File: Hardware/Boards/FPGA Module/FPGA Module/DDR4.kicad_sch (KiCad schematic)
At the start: 0 parts

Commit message: FPGA Module Schematic work
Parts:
- added U17: MT40A512M16LY-075:E, FPGA Module:BGA96C80P9X16_750X1350X120, symbol FPGA Module:MT40A512M16LY-075{colon}E

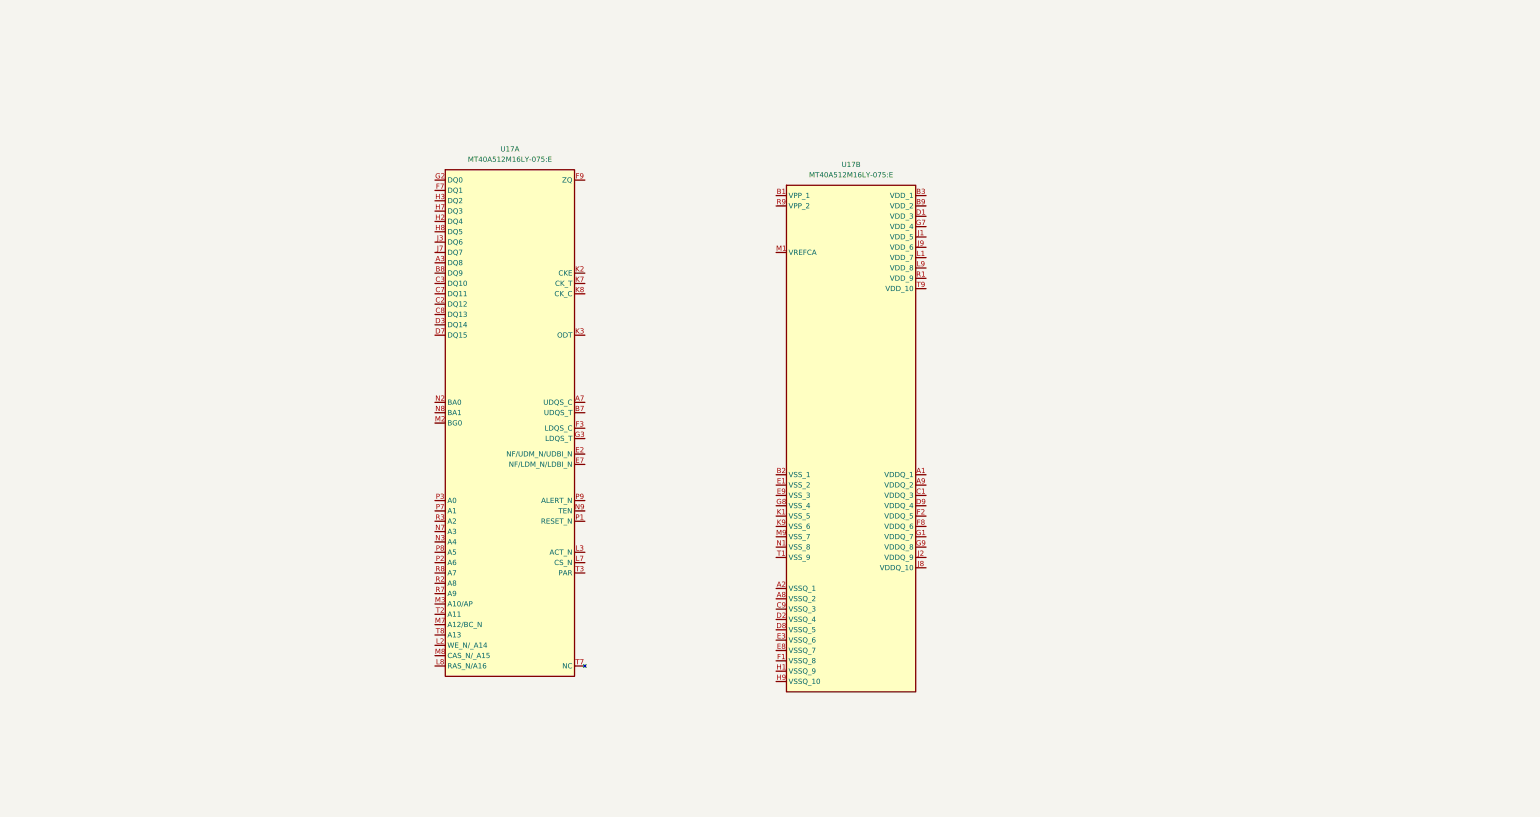
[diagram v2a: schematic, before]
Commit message: Added DDR sch in FPGA module
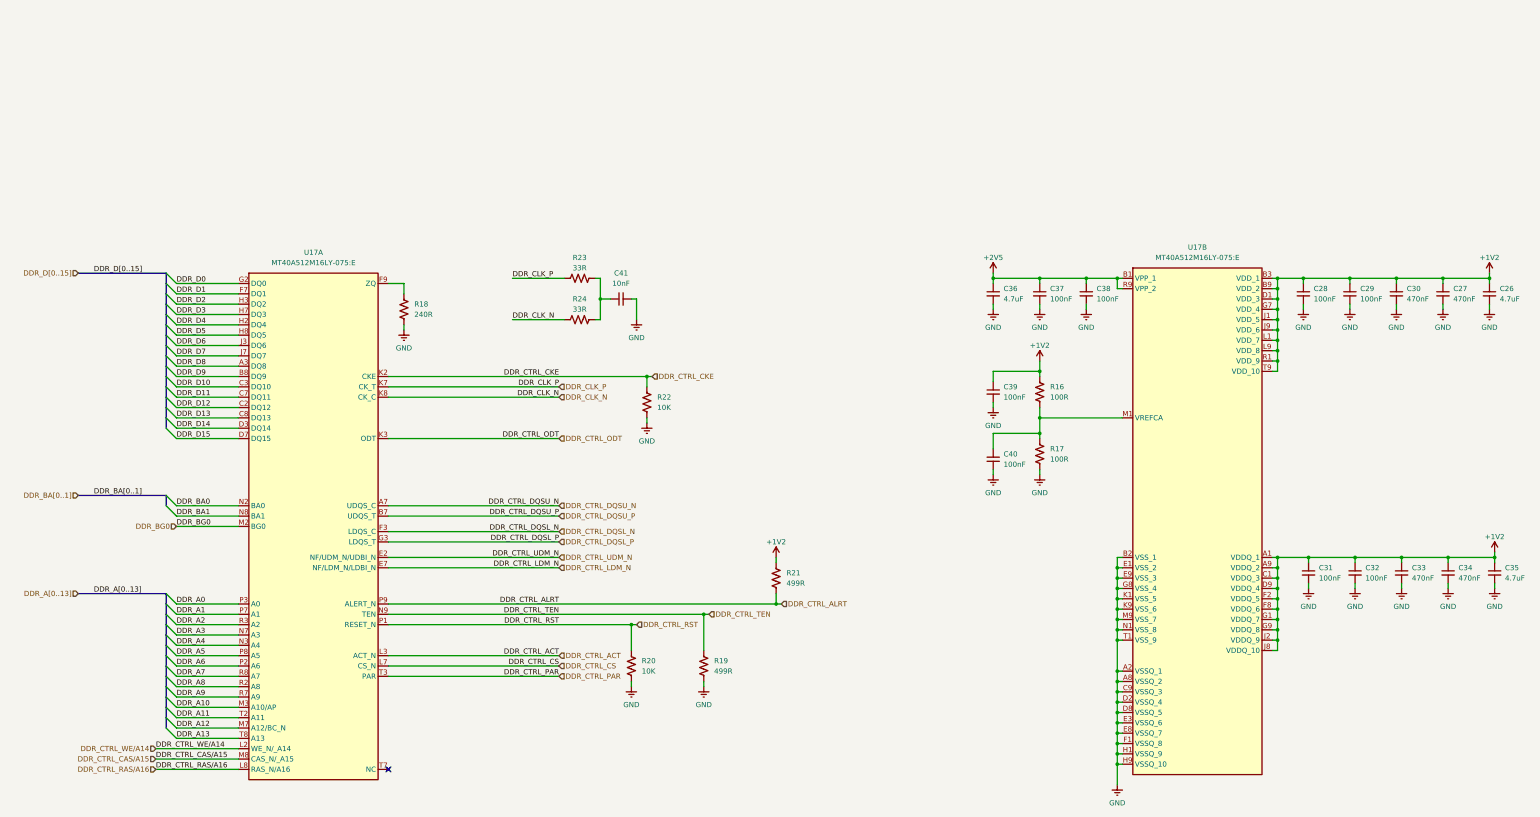
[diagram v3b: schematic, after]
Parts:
- added C26, C35, C36: 4.7uF, Capacitor_SMD:C_0402_1005Metric, symbol Device:C_Small
- added C27, C30, C33, C34: 470nF, Capacitor_SMD:C_0402_1005Metric, symbol Device:C_Small
- added C28, C29, C31, C32, C37, C38, C39, C40: 100nF, Capacitor_SMD:C_0402_1005Metric, symbol Device:C_Small
- added C41: 10nF, Capacitor_SMD:C_0402_1005Metric, symbol Device:C_Small
- added R16, R17: 100R, Resistor_SMD:R_0402_1005Metric, symbol Device:R_US
- added R18: 240R, Resistor_SMD:R_0402_1005Metric, symbol Device:R_US
- added R19, R21: 499R, Resistor_SMD:R_0402_1005Metric, symbol Device:R_US
- added R20, R22: 10K, Resistor_SMD:R_0402_1005Metric, symbol Device:R_US
- added R23, R24: 33R, Resistor_SMD:R_0402_1005Metric, symbol Device:R_US
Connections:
- net DDR_D8: now reaches U17.A3 (DQ8)
- net DDR_CTRL_DQSU_N: now reaches U17.A7 (UDQS_C)
- net DDR_CTRL_DQSU_P: now reaches U17.B7 (UDQS_T)
- net DDR_D9: now reaches U17.B8 (DQ9)
- net DDR_D12: now reaches U17.C2 (DQ12)
- net DDR_D10: now reaches U17.C3 (DQ10)
- net DDR_D11: now reaches U17.C7 (DQ11)
- net DDR_D13: now reaches U17.C8 (DQ13)
- net DDR_D14: now reaches U17.D3 (DQ14)
- net DDR_D15: now reaches U17.D7 (DQ15)
- net DDR_CTRL_UDM_N: now reaches U17.E2 (NF/UDM_N/UDBI_N)
- net DDR_CTRL_LDM_N: now reaches U17.E7 (NF/LDM_N/LDBI_N)
- net DDR_CTRL_DQSL_N: now reaches U17.F3 (LDQS_C)
- net DDR_D1: now reaches U17.F7 (DQ1)
- net at U17.F9 (ZQ): now also R18.2
- net DDR_D0: now reaches U17.G2 (DQ0)
- net DDR_CTRL_DQSL_P: now reaches U17.G3 (LDQS_T)
- net DDR_D4: now reaches U17.H2 (DQ4)
- net DDR_D2: now reaches U17.H3 (DQ2)
- net DDR_D3: now reaches U17.H7 (DQ3)
- net DDR_D5: now reaches U17.H8 (DQ5)
- net DDR_D6: now reaches U17.J3 (DQ6)
- net DDR_D7: now reaches U17.J7 (DQ7)
- net DDR_CTRL_CKE: now reaches U17.K2 (CKE)
- net DDR_CTRL_CKE: now also R22.2
- net DDR_CTRL_ODT: now reaches U17.K3 (ODT)
- net DDR_CLK_P: now reaches U17.K7 (CK_T)
- net DDR_CLK_P: now also R23.2
- net DDR_CLK_N: now reaches U17.K8 (CK_C)
- net DDR_CLK_N: now also R24.2
- net DDR_CTRL_WE/A14: now reaches U17.L2 (WE_N/_A14)
- net DDR_CTRL_ACT: now reaches U17.L3 (ACT_N)
- net DDR_CTRL_CS: now reaches U17.L7 (CS_N)
- net DDR_CTRL_RAS/A16: now reaches U17.L8 (RAS_N/A16)
- net DDR_BG0: now reaches U17.M2 (BG0)
- net DDR_A10: now reaches U17.M3 (A10/AP)
- net DDR_A12: now reaches U17.M7 (A12/BC_N)
- net DDR_CTRL_CAS/A15: now reaches U17.M8 (CAS_N/_A15)
- net DDR_BA0: now reaches U17.N2 (BA0)
- net DDR_A4: now reaches U17.N3 (A4)
- net DDR_A3: now reaches U17.N7 (A3)
- net DDR_BA1: now reaches U17.N8 (BA1)
- net DDR_CTRL_TEN: now reaches U17.N9 (TEN)
- net DDR_CTRL_TEN: now also R19.2
- net DDR_CTRL_RST: now reaches U17.P1 (RESET_N)
- net DDR_CTRL_RST: now also R20.2
- net DDR_A6: now reaches U17.P2 (A6)
- net DDR_A0: now reaches U17.P3 (A0)
- net DDR_A1: now reaches U17.P7 (A1)
- net DDR_A5: now reaches U17.P8 (A5)
- net DDR_CTRL_ALRT: now reaches U17.P9 (ALERT_N)
- net DDR_CTRL_ALRT: now also R21.1
- net DDR_A8: now reaches U17.R2 (A8)
- net DDR_A2: now reaches U17.R3 (A2)
- net DDR_A9: now reaches U17.R7 (A9)
- net DDR_A7: now reaches U17.R8 (A7)
- net DDR_A11: now reaches U17.T2 (A11)
- net DDR_CTRL_PAR: now reaches U17.T3 (PAR)
- net DDR_A13: now reaches U17.T8 (A13)
- net +1V2: now reaches U17.A1 (VDDQ_1)
- net +1V2: now also U17.A9 (VDDQ_2), U17.B3 (VDD_1), U17.B9 (VDD_2), U17.C1 (VDDQ_3), U17.D1 (VDD_3), U17.D9 (VDDQ_4), U17.F2 (VDDQ_5), U17.F8 (VDDQ_6), U17.G1 (VDDQ_7), U17.G7 (VDD_4), U17.G9 (VDDQ_8), U17.J1 (VDD_5), U17.J2 (VDDQ_9), U17.J8 (VDDQ_10), U17.J9 (VDD_6), U17.L1 (VDD_7), U17.L9 (VDD_8), U17.R1 (VDD_9), U17.T9 (VDD_10), C26.1, C27.1, C28.1, C29.1, C30.1, C31.1, C32.1, C33.1, C34.1, C35.1, C39.1, R16.2, R21.2
- net GND: now reaches U17.A2 (VSSQ_1)
- net GND: now also U17.A8 (VSSQ_2), U17.B2 (VSS_1), U17.C9 (VSSQ_3), U17.D2 (VSSQ_4), U17.D8 (VSSQ_5), U17.E1 (VSS_2), U17.E3 (VSSQ_6), U17.E8 (VSSQ_7), U17.E9 (VSS_3), U17.F1 (VSSQ_8), U17.G8 (VSS_4), U17.H1 (VSSQ_9), U17.H9 (VSSQ_10), U17.K1 (VSS_5), U17.K9 (VSS_6), U17.M9 (VSS_7), U17.N1 (VSS_8), U17.T1 (VSS_9), C26.2, C27.2, C28.2, C29.2, C30.2, C31.2, C32.2, C33.2, C34.2, C35.2, C36.2, C37.2, C38.2, C39.2, C40.2, C41.2, R17.1, R18.1, R19.1, R20.1, R22.1
- net +2V5: now reaches U17.B1 (VPP_1)
- net +2V5: now also U17.R9 (VPP_2), C36.1, C37.1, C38.1
- net at U17.M1 (VREFCA): now also C40.1, R16.1, R17.2
- new net: C41.1, R23.1, R24.1
- no-connect marks 0 -> 1
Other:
- moved on the sheet: U17A, U17B

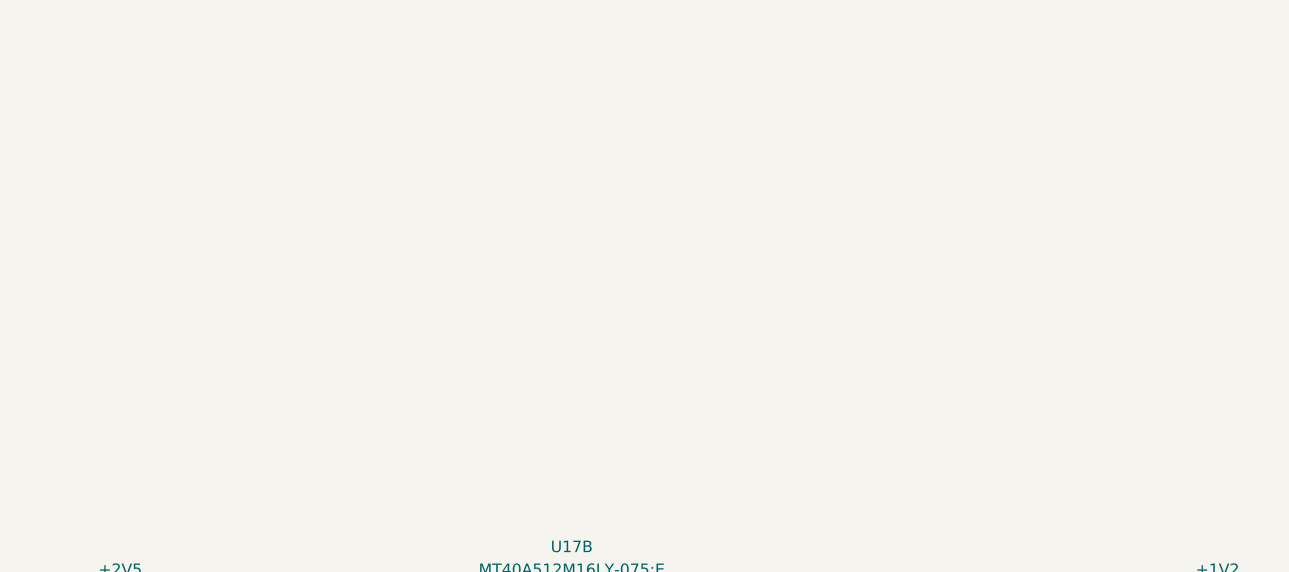
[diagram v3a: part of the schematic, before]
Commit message: updated fpga module schematics
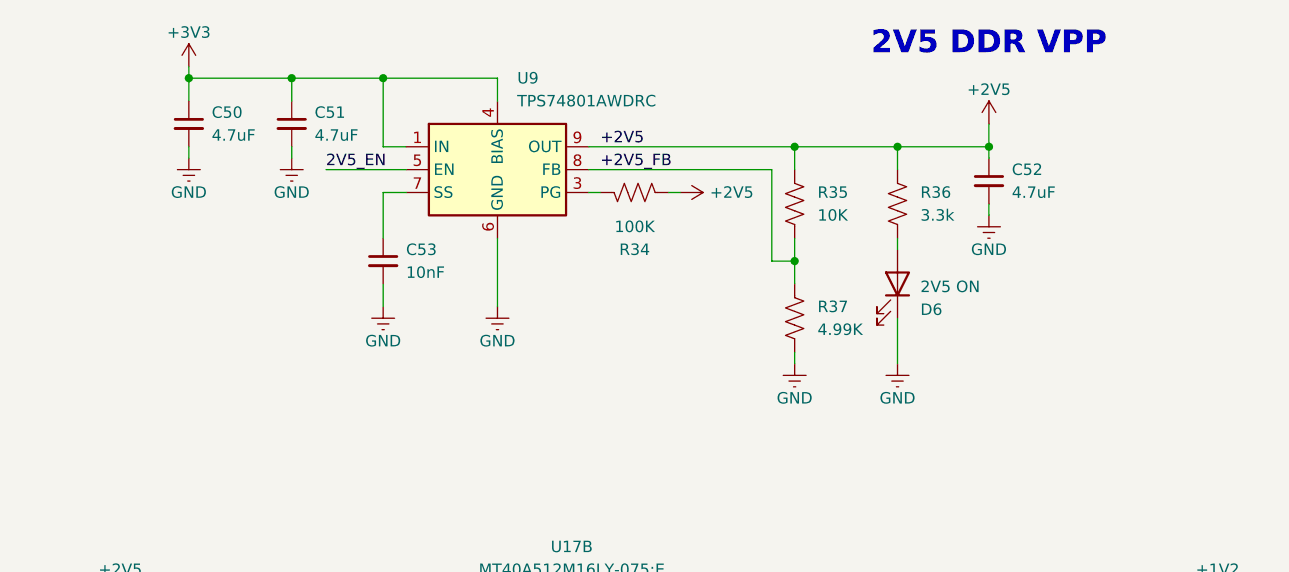
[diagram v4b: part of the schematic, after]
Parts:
- added C50, C51, C52: 4.7uF, Capacitor_SMD:C_0402_1005Metric, symbol Device:C_Small
- added C53: 10nF, Capacitor_SMD:C_0402_1005Metric, symbol Device:C_Small
- added D6: 2V5 ON, LED_SMD:LED_0603_1608Metric, symbol Device:LED
- added R34: 100K, Resistor_SMD:R_0402_1005Metric, symbol Device:R_US
- added R35: 10K, Resistor_SMD:R_0402_1005Metric, symbol Device:R_US
- added R36: 3.3k, Resistor_SMD:R_0402_1005Metric, symbol Device:R_US
- added R37: 4.99K, Resistor_SMD:R_0402_1005Metric, symbol Device:R_US
- added U9: TPS74801AWDRC, Package_SON:VSON-10-1EP_3x3mm_P0.5mm_EP1.65x2.4mm_ThermalVias, symbol Regulator_Linear:TPS74801AWDRC
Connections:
- net +2V5: now also C52.1, R34.2, R35.1, R36.1, U9.10 (OUT), U9.9 (OUT)
- net GND: now also C50.2, C51.2, C52.2, C53.2, D6.1 (K), R37.2, U9.11 (GND), U9.6 (GND)
- new net: C53.1, U9.7 (SS)
- new net: R34.1, U9.3 (PG)
- new net: D6.2 (A), R36.2
- new net +2V5_FB: R35.2, R37.1, U9.8 (FB)
- new net +3V3: C50.1, C51.1, U9.1 (IN), U9.2 (IN), U9.4 (BIAS)
- new net 2V5_EN: U9.5 (EN)
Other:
- note added: "2V5 DDR VPP"
